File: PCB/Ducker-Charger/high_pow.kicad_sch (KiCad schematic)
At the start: 0 parts

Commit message: feat: added High power main sections
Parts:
- added C1: 10u, symbol Device:C
- added C_BST1, C_BST2: 100n, symbol Device:C
- added L1: 10u, symbol Device:L
- added Q1, Q2, Q3, Q4: NCE3080K, EasyEDA:TO-252-2_L6.6-W6.1-P4.57-LS9.9-TL-CW, symbol EasyEDA:NCE3080K
- added R1: 10m, symbol Device:R
- added R2: 10K, symbol Device:R
- added TH1: Thermistor_NTC, symbol Device:Thermistor_NTC
- added U1: IP5389_CN_AACD_WC4QD, EasyEDA:QFN-64_L8.0-W8.0-P0.40-TL-EP6.2, symbol EasyEDA:IP5389_CN_AACD_WC4QD
- added USBC1: TYPE-C-31-M-12, EasyEDA:USB-C_SMD-TYPE-C-31-M-12_1, symbol EasyEDA:TYPE-C-31-M-12
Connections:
- new net BST1: C_BST1.1, U1.22 (BST1)
- new net BST2: C_BST2.1
- new net CC1: U1.54 (CC1), USBC1.A5 (CC1)
- new net CC2: U1.51 (CC2), USBC1.B5 (CC2)
- new net CONF_SETT: R2.1, U1.41 (VSET)
- new net DN: U1.53 (DMC), USBC1.A7 (DN1), USBC1.B7 (DN2)
- new net DP: U1.52 (DPC), USBC1.A6 (DP1), USBC1.B6 (DP2)
- new net GND: C1.2, Q2.3 (S), Q4.3 (S), R2.2, TH1.2, USBC1.1 (EH), USBC1.2 (EH), USBC1.3 (EH), USBC1.4 (EH), USBC1.A1B12 (GND), USBC1.B1A12 (GND)
- new net HG1: Q1.1 (G), U1.21 (HG1)
- new net HG2: Q3.1 (G), U1.28 (HG2)
- new net LG1: Q2.1 (G), U1.24 (LG1)
- new net LG2: Q4.1 (G), U1.25 (LG2)
- new net LX1: C_BST1.2, L1.1, Q1.3 (S), Q2.2 (D), U1.23 (LX1)
- new net LX2: C_BST2.2, L1.2, Q3.3 (S), Q4.2 (D), U1.26 (LX2)
- new net PD_ON: U1.36 (KEY)
- new net SCL: U1.55 (DPA1)
- new net SDA: U1.56 (DMA1)
- new net VBUS: Q3.2 (D), USBC1.A4B9 (VBUS), USBC1.B4A9 (VBUS)
- new net VCC5V: C1.1, U1.17 (VIO), U1.34 (VCC5V)
- new net V_SYS_A: Q1.2 (D), R1.2, U1.10 (VIN), U1.11 (VING), U1.12 (VIN_I), U1.19 (CSN1)
- new net V_SYS_B: R1.1, U1.18 (CSP1), U1.32 (BAT)
- new net temp: TH1.1, U1.50 (NTC)
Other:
- note added: "BOOTSTRAP & DECOUPLING"
- note added: "BUCK-BOOST POWER STAGE"
- note added: "HARDWARE CONFIG"
- note added: "HARDWARE SAFETY"
- note added: "POWER MANAGEMENT IC"
- note added: "Rshunt"
- note added: "USB-C INTERFACE"

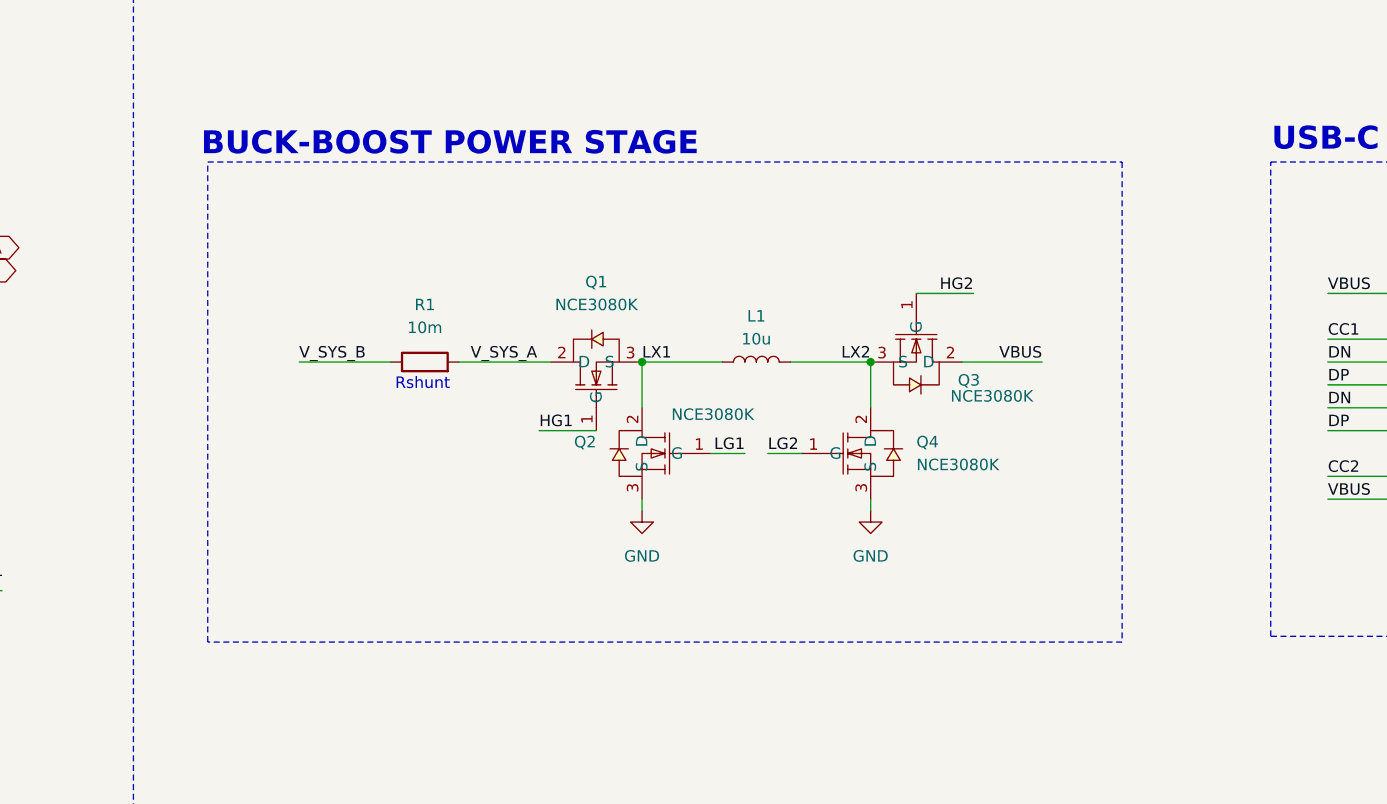
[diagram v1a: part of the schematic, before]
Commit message: feat: added capacitors to BUCK-BOOST POWER STAGE
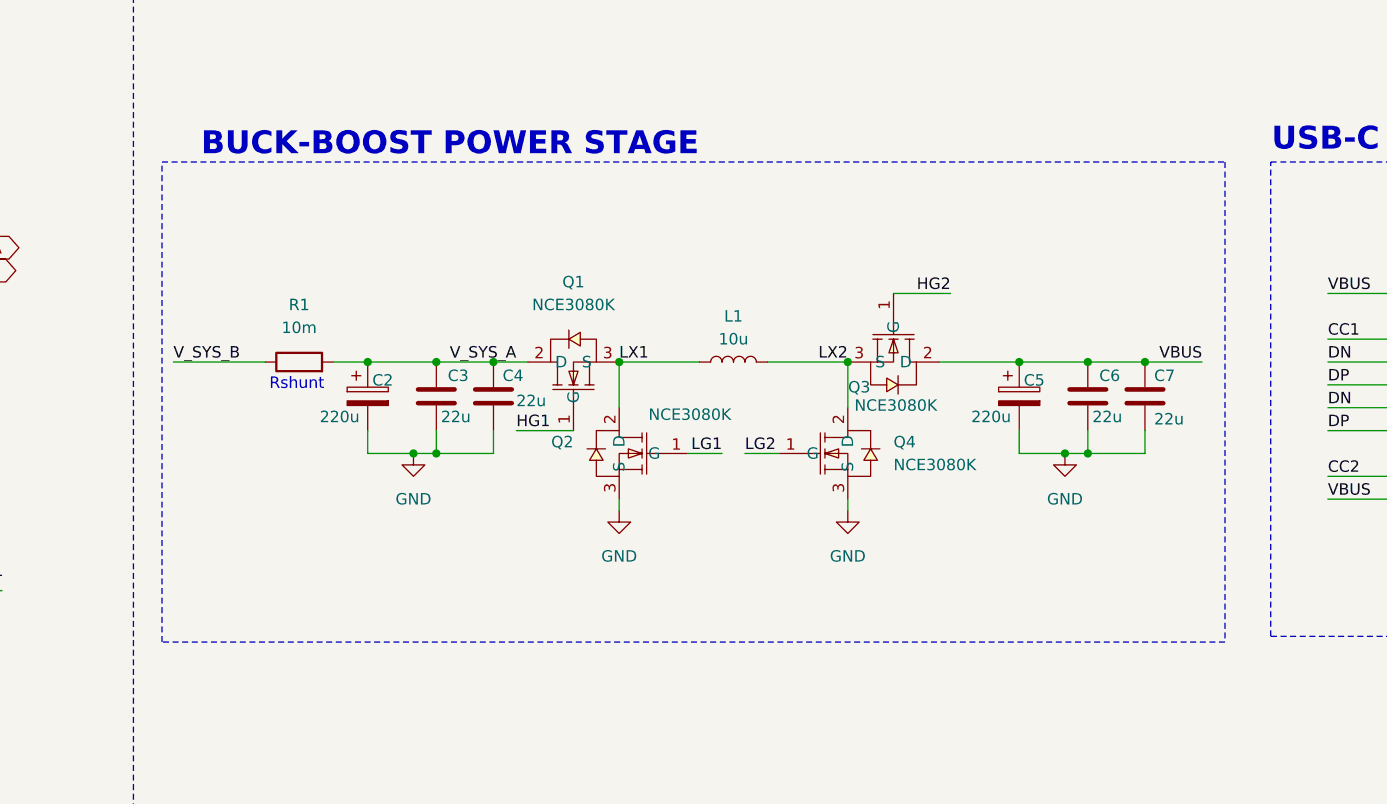
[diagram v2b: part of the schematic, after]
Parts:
- added C2, C5: 220u, symbol Device:C_Polarized
- added C3, C4, C6, C7: 22u, symbol Device:C
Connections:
- net GND: now also C2.2, C3.2, C4.2, C5.2, C6.2, C7.2
- net VBUS: now also C5.1, C6.1, C7.1
- net V_SYS_A: now also C2.1, C3.1, C4.1
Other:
- moved on the sheet: L1, Q1, Q2, Q3, Q4, R1

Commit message: feat: completed High power stage
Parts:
- added C8: 100n, symbol Device:C
- added D1: USBLC6-4SC6, EasyEDA:SOT-23-6_L2.9-W1.6-P0.95-LS2.8-BL, symbol EasyEDA:USBLC6-4SC6
- added D2: SMBJ22A-E3/52, EasyEDA:SMB_L4.3-W3.6-LS5.4-RD, symbol EasyEDA:SMBJ22A-E3_52
- added R3, R4, R5, R6: 10, symbol Device:R
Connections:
- net CC1: now also D1.4
- net CC2: now also D1.6
- net DN: now also D1.3
- net DP: now also D1.1
- net GND: now also U1.16 (AGND), U1.59 (VOUT1_I), U1.64 (VOUT2_I), U1.65 (EP), C8.2, D1.2, D2.2 (A)
- net HG1: now also R3.1; no longer Q1.1 (G)
- net HG2: now also R4.2; no longer Q3.1 (G)
- net LG1: now also R5.1; no longer Q2.1 (G)
- net LG2: now also R6.1; no longer Q4.1 (G)
- net VBUS: now also D1.5, D2.1 (C)
- net VCC5V: no longer U1.17 (VIO)
- net PCIN: now reaches U1.20 (PCIN)
- net PCIN: now also C8.1
- new net: Q2.1 (G), R5.2
- new net: Q1.1 (G), R3.2
- new net: Q4.1 (G), R6.2
- new net: Q3.1 (G), R4.1
- new net +3V3: U1.17 (VIO)
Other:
- note added: "30V"
- note added: "ESD PROTECTION"
- note added: "NB: I pin AGND e GND sono collegati elettricamente nello schematico per garantire il riferimento DC. Nel PCB, devono essere uniti in un UNICO punto (Star Ground), preferibilmente sotto il Pad Termico (EP) del chip, per isolare la logica analogica dai disturbi di potenza."
- note added: "pullup must be added 4k7 - 3v3"
- moved on the sheet: C1, C2, C3, C4, C5, C6, C7, C_BST1, C_BST2, L1, Q1, Q2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

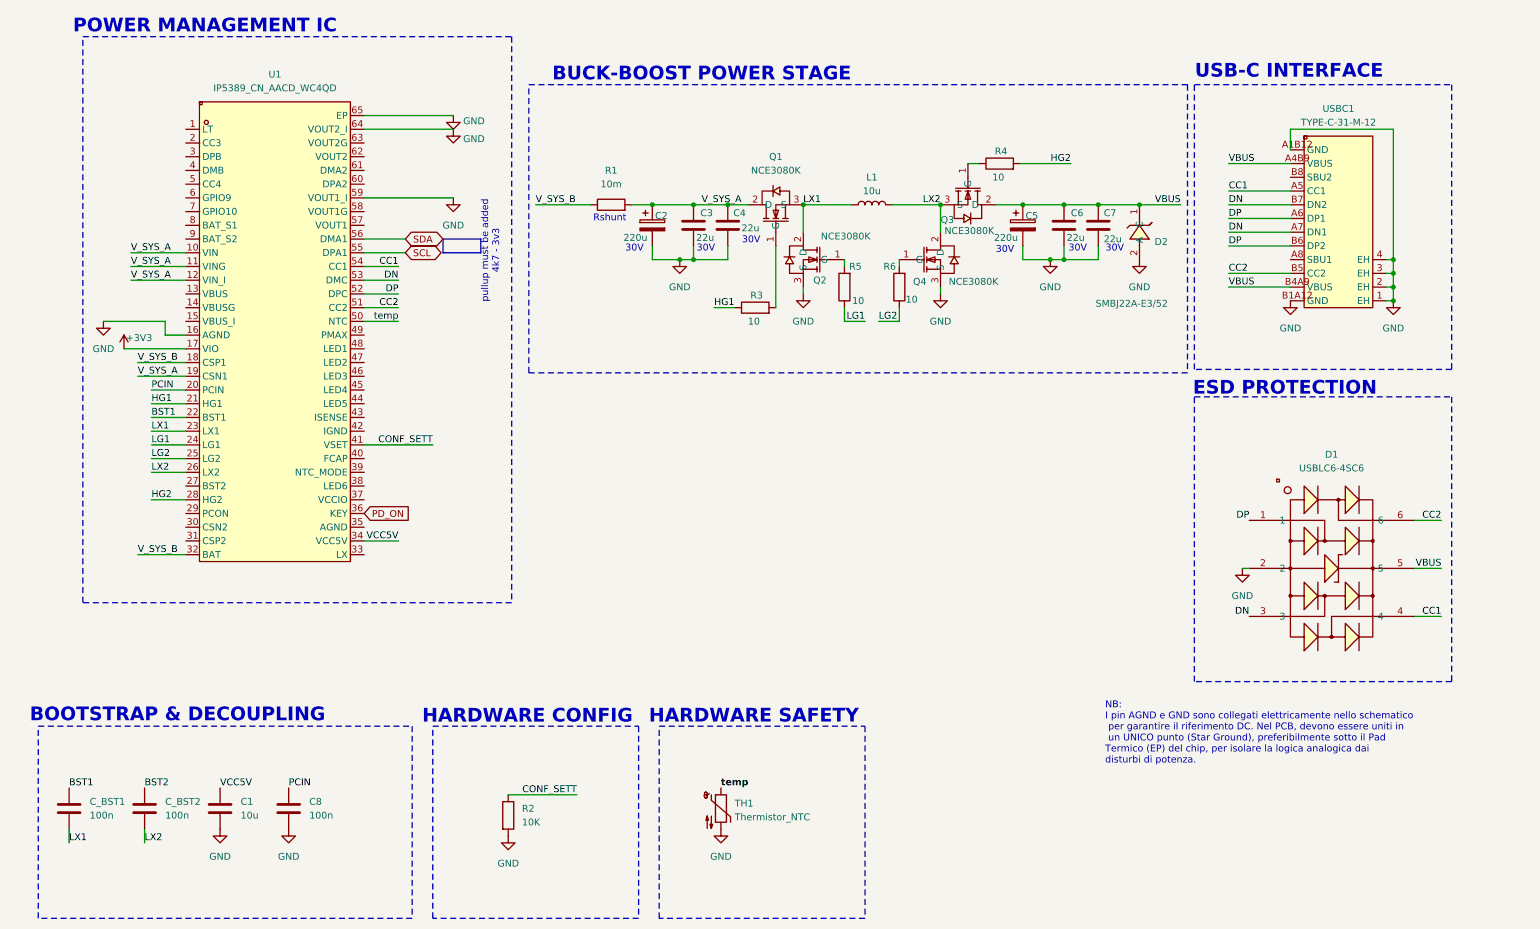
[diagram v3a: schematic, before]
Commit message: fix: unconnected pins, wrong connections
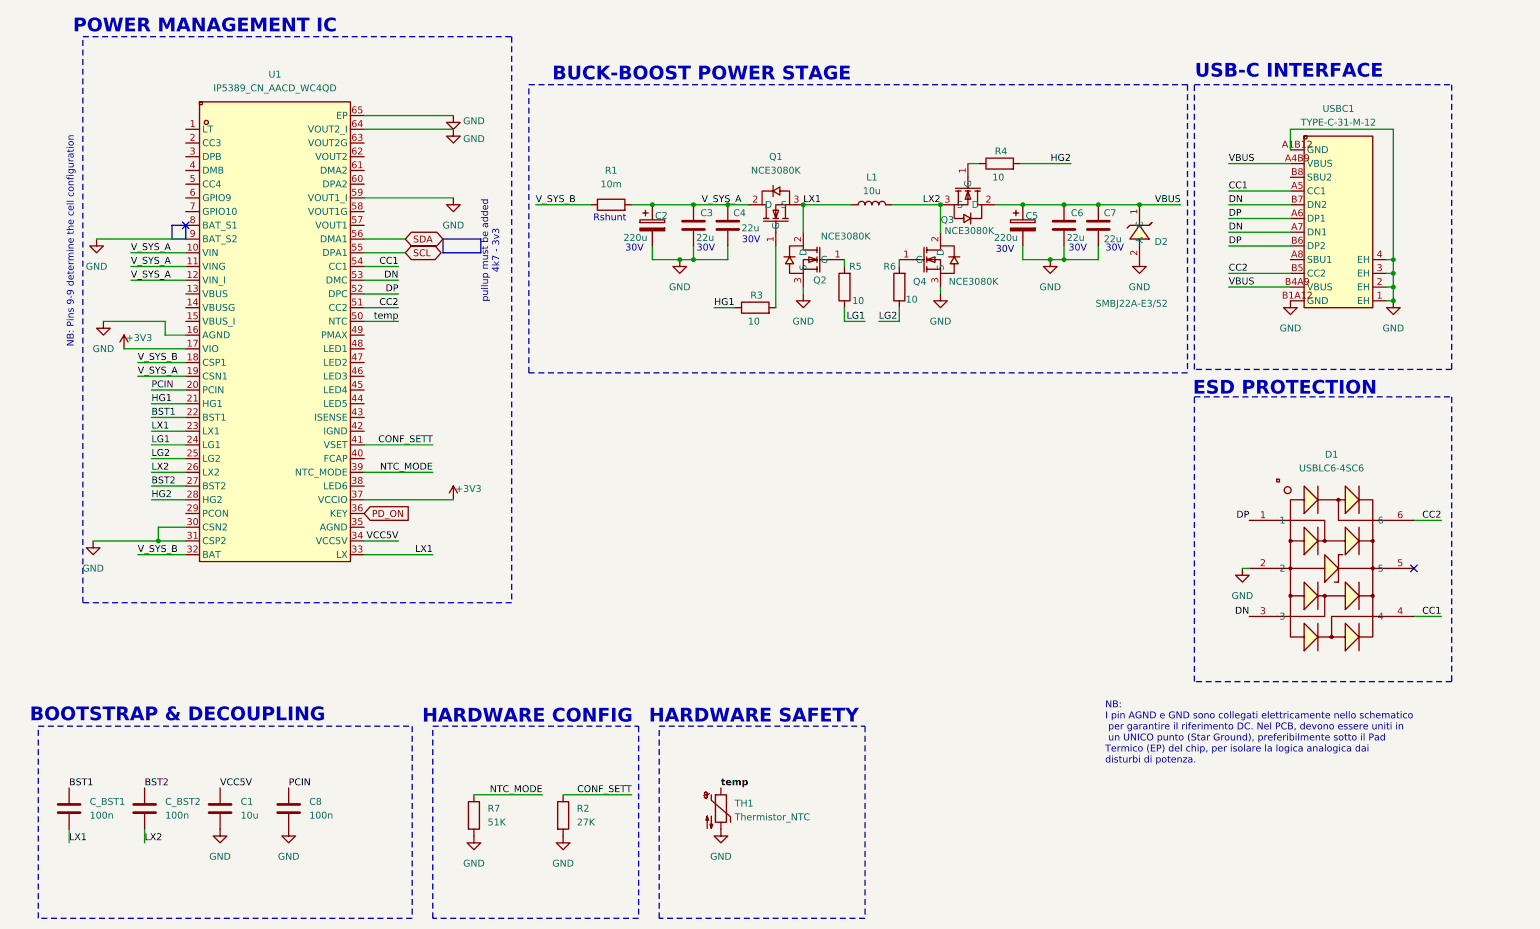
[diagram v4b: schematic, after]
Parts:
- added R7: 51K, symbol Device:R
- R2: value 10K -> 27K
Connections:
- net +3V3: now also U1.37 (VCCIO)
- net BST2: now also U1.27 (BST2)
- net GND: now also U1.30 (CSN2), U1.31 (CSP2), U1.9 (BAT_S2), R7.2
- net LX1: now also U1.33 (LX)
- net VBUS: no longer D1.5
- net NTC_MODE: now reaches U1.39 (NTC_MODE)
- net NTC_MODE: now also R7.1
- no-connect marks 0 -> 2
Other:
- note added: "NB: Pins 9-9 determine the cell configuration"
- moved on the sheet: R2
